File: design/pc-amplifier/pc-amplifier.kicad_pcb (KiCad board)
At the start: 2 copper layers, 136 parts, among them J1 PJ307, J2 DC-005, J3 PJ307, J4 AV-8.4-3, J5 AV-8.4-3, K1 HK19F-DC-12-SHG, Q1 BC858, Q2 BC817, Q3 BC817, Q4 BC817, SW1 6mm Tactile SW, SW2 6mm Tactile SW, SW3 6mm Tactile SW, SW4 6mm Tactile SW, U1 TDA8425, U2 NE5532, U3 NE5532, U4 NE5532, U5 YDA138, U6 MC78L05, U7 AC6939-MODULE

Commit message: Initial version of the PCB.
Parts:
- C2, C3, C30, C4, C56, D4, Q1, Q2, Q3, Q4, R23, R24, R25, R26, R27, R28, R29, TP3, TP4, TP5, U6: moved to B.Cu
- C20, C21, C29, C32: moved to F.Cu
- R1, R2: footprint Resistor_SMD:R_0805_2012Metric_Pad1.20x1.40mm_HandSolder -> Resistor_THT:R_Axial_DIN0204_L3.6mm_D1.6mm_P1.90mm_Vertical
- moved U5 227.3 mm to (157.1, 98.9)
- moved L6 222.6 mm to (147.5, 109.8), turned to 180 degrees
- moved K1 220.6 mm to (188.2, 93.1), turned to 90 degrees
- moved L1 217.7 mm to (184.2, 100.9), turned to 90 degrees
- moved C35 212.9 mm to (168.1, 106.1)
- moved R25 211.1 mm to (182.5, 105.1), turned to 90 degrees
- moved Q2 209.9 mm to (181.5, 100.9), turned to 90 degrees
- moved U6 209.6 mm to (145.0, 103.8)
- moved JP3 209.5 mm to (161.8, 113.2), turned to 90 degrees
- moved C54 206.4 mm to (136.2, 110.3), turned to -90 degrees
- moved D4 205.1 mm to (184.2, 96.8), turned to 180 degrees
- moved R23 205.0 mm to (90.4, 101.1), turned to -90 degrees
- moved C38 203.4 mm to (168.8, 102.1)
- moved C33 203.3 mm to (174.1, 108.5), turned to -90 degrees
- moved C56 201.3 mm to (141.0, 104.5), turned to 90 degrees
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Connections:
- Q2 pad 2: GNDA -> GND
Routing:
- net GNDA: track 0.00 -> 828.6 mm, vias 0 -> 29
- net +12V: track 0.00 -> 432.2 mm
- net GNDD: track 0.00 -> 418.3 mm, vias 0 -> 7
- net /control-module/SPK-SELECT: track 0.00 -> 173.4 mm, vias 0 -> 3
- net Net-(Q1-Pad3): track 0.00 -> 124.2 mm, vias 0 -> 2
- net +12VA: track 0.00 -> 111.3 mm
- net +5V: track 0.00 -> 103.5 mm, vias 0 -> 1
- net +5VD: track 0.00 -> 101.8 mm, vias 0 -> 6
- net /control-module/MUTE: track 0.00 -> 100.9 mm, vias 0 -> 1
- net /audio-processor/AF-ANALYZER-L: track 0.00 -> 90.9 mm, vias 0 -> 4
- net GND: track 0.00 -> 85.9 mm, vias 0 -> 1
- net /audio-processor/SDA: track 0.00 -> 80.4 mm, vias 0 -> 3
- net /audio-processor/SCL: track 0.00 -> 71.5 mm, vias 0 -> 3
- net /audio-processor/BT-RIGHT: track 0.00 -> 70.2 mm
- net /power-amplifier/AF-HP-OUT-R: track 0.00 -> 61.3 mm
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
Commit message: Routed PCB design for REV 1.0.
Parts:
- added G***: LOGO, pc-amplifier:pcbway, F.Cu at (110.0, 107.0)
- added H1: 2.5mm hole, MountingHole:MountingHole_2.5mm_Pad, F.Cu at (198.2, 111.6)
- added H2: 2.5mm hole, MountingHole:MountingHole_2.5mm_Pad, F.Cu at (172.4, 66.6)
- added REF**: OSHW-Logo2_9.8x8mm_SilkScreen, Symbol:OSHW-Logo2_9.8x8mm_SilkScreen, B.Cu at (174.3, 87.6)
- moved TP2 3.32 mm to (134.0, 93.3)
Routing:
- net GNDA: track 828.6 -> 221.9 mm, vias 29 -> 62
- net GNDD: track 418.3 -> 333.2 mm, vias 7 -> 46
- net Net-(C53-Pad1): track 25.4 -> 45.8 mm
- net Net-(C41-Pad1): track 50.7 -> 68.7 mm
- net Net-(L5-Pad1): track 32.3 -> 40.1 mm
- net +5VD: track 101.8 -> 109.3 mm
- net +12V: track 432.2 -> 426.5 mm
- net +12VA: track 111.3 -> 116.9 mm
- net Net-(C20-Pad1): track 8.79 -> 13.1 mm
- net Net-(DS1-Pad15): track 3.44 -> 6.87 mm
- net Net-(C26-Pad1): track 3.11 -> 6.22 mm
- net /audio-processor/AF-ANALYZER-R: track 41.2 -> 43.1 mm
- net /power-amplifier/HEADPHONE-R: track 22.7 -> 20.8 mm
- net /power-amplifier/AF-HP-OUT-R: track 61.3 -> 60.2 mm
- net /power-amplifier/HEADPHONE-L: track 9.32 -> 10.1 mm
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- added copper zone on B.Cu, net GNDA
- added copper zone on F.Cu, net GNDA
- added copper zone on B.Cu, net GNDD
- added copper zone on F.Cu, net GNDD
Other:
- board outline added: 149.9 x 55.9 mm
- board text added: "12V-DC"
- board text added: "36dB 30dB 24dB 18dB"
- board text added: "ARDUINO NANO 3"
- board text added: "BLUETOOTH MODULE"
- board text added: "DILSHAN R. JAYAKODY"
- board text added: "DOWN"
- board text added: "GAIN0"
- board text added: "GAIN1"
- board text added: "H"
- board text added: "H H"
- board text added: "H L"
- board text added: "H.PHONE"
- board text added: "L"
- board text added: "L H"
- board text added: "L L"
- board text added: "LINE IN"
- board text added: "Licensed under CERN-OHL-W 2.0"
- board text added: "MUTE"
- board text added: "OPT"
- board text added: "R"
- board text added: "REV 1.0"
- board text added: "SPK"
- board text added: "UP"
- board text added: "jayakody2000lk.blogspot.com"
- board text added: "sponsored by"

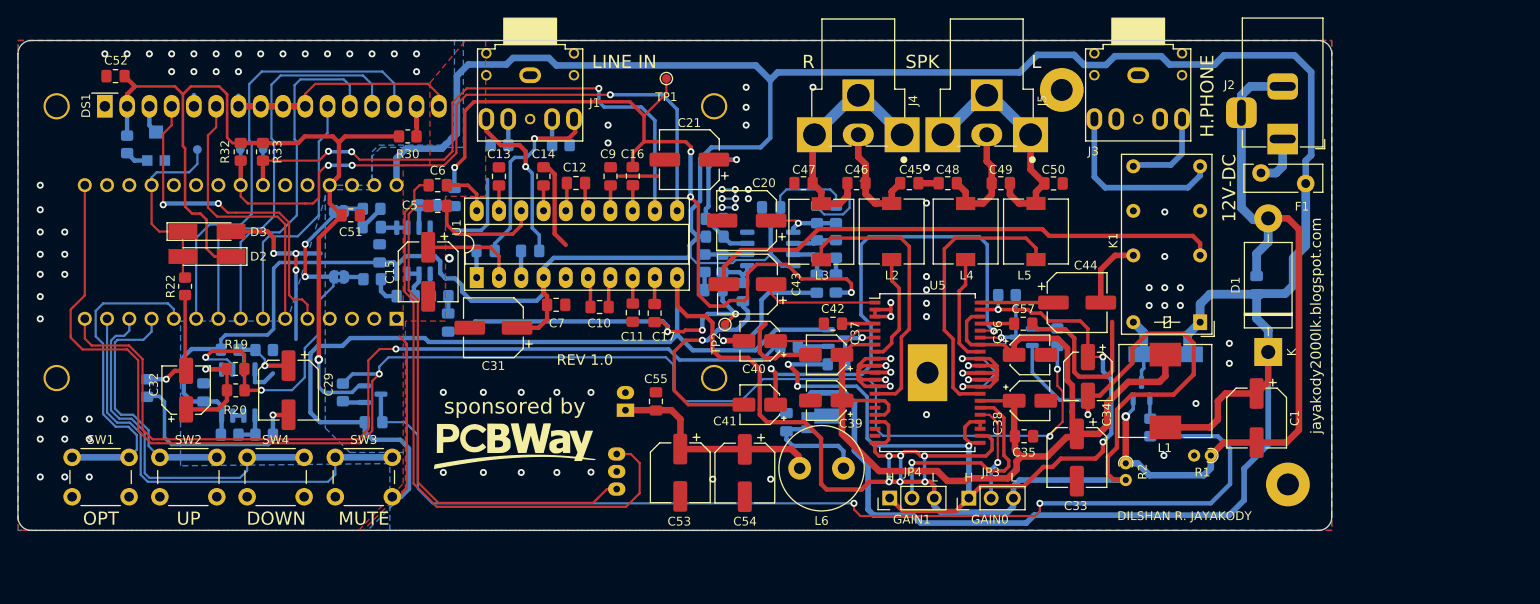
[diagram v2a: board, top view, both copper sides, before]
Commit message: Add page settings to PCB and schematic.
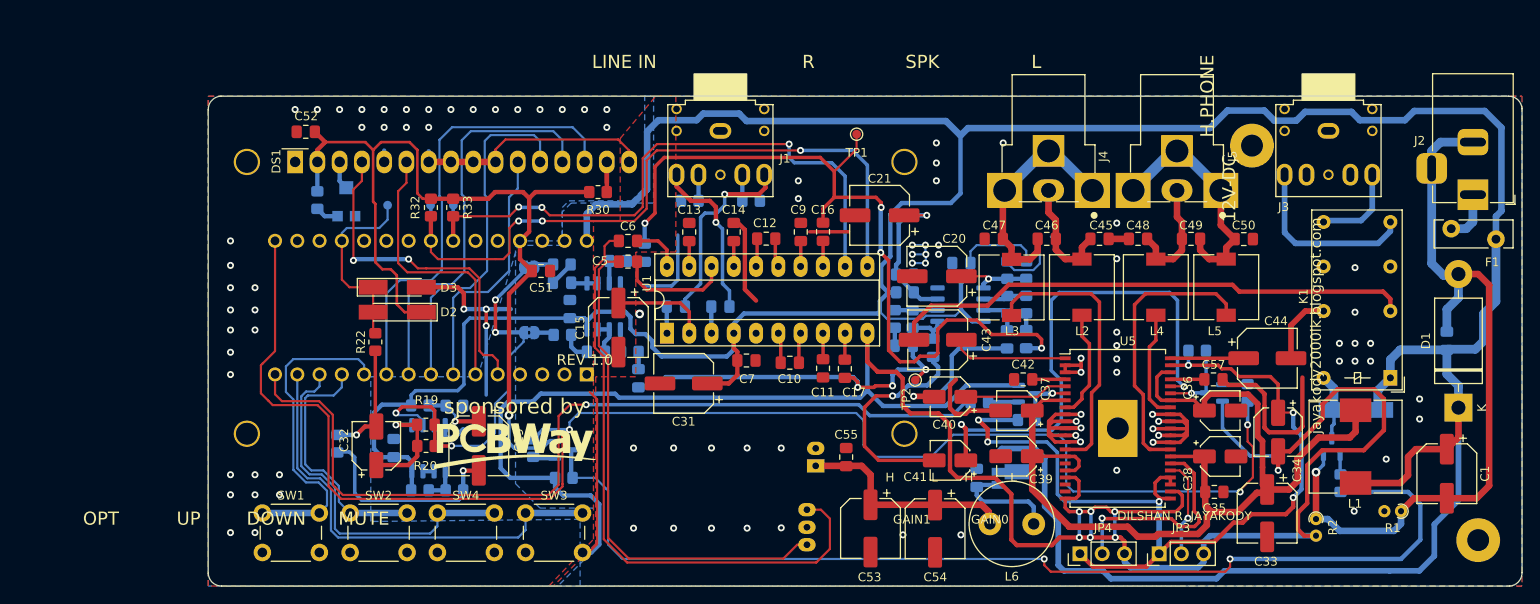
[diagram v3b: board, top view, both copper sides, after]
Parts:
- moved C1 22.6 mm to (216.3, 110.4)
- moved C18 22.6 mm to (168.3, 95.0)
- moved C33 22.6 mm to (195.8, 114.9)
- moved C34 22.6 mm to (197.1, 105.6)
- moved C35 22.6 mm to (189.8, 112.5)
- moved C39 22.6 mm to (167.2, 108.4)
- moved C53 22.6 mm to (150.6, 116.6)
- moved D1 22.6 mm to (217.7, 102.8)
- moved H1 22.6 mm to (219.9, 118.0)
- moved J3 22.6 mm to (202.8, 74.3)
- moved Q3 22.6 mm to (189.8, 101.2)
- moved R2 22.6 mm to (201.4, 115.5)
- moved R3 22.6 mm to (168.3, 91.1)
- moved R34 22.6 mm to (137.0, 79.2)
- moved R5 22.6 mm to (168.3, 87.1)
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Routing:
- net GNDA: track 221.9 -> 202.0 mm

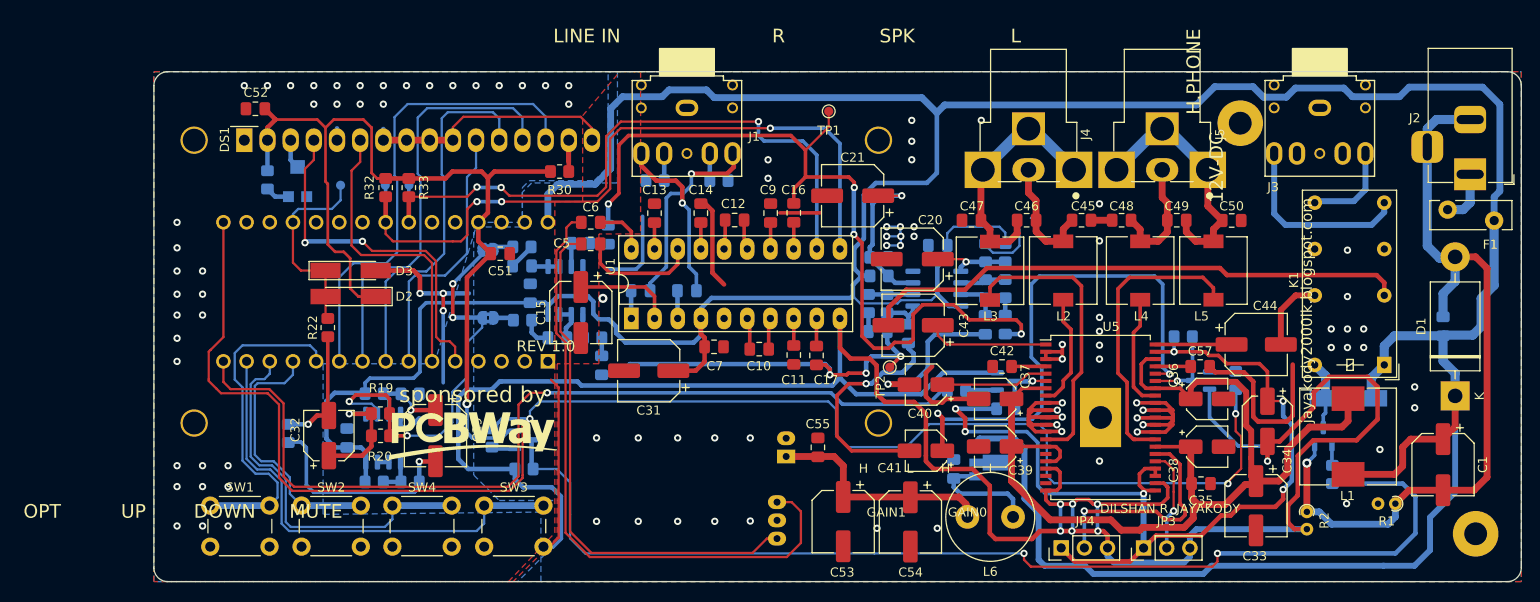
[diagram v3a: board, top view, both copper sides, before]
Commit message: Fix silkscreen offset issues in front layer.
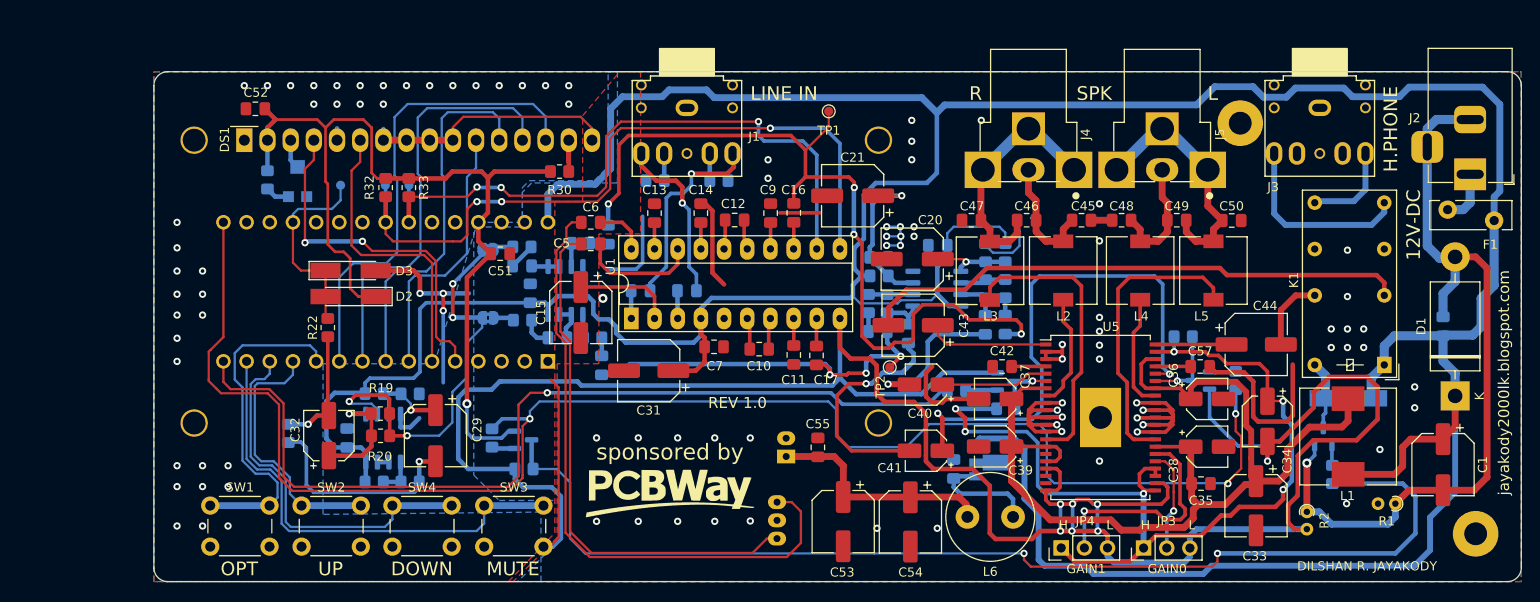
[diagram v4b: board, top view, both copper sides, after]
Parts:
- moved G*** 22.5 mm to (131.6, 113.3)
